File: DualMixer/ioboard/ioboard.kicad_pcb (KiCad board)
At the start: 2 copper layers, 35.6 x 107.9 mm, 22 parts, among them J1 IN_A1, J10 IN_B4, J11 OUTB, J13 Conn_01x03_Male, J2 IN_A2, J3 IN_A3, J4 OUTA, J5 Conn_02x07_Odd_Even, J6 IN_A4, J7 IN_B1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

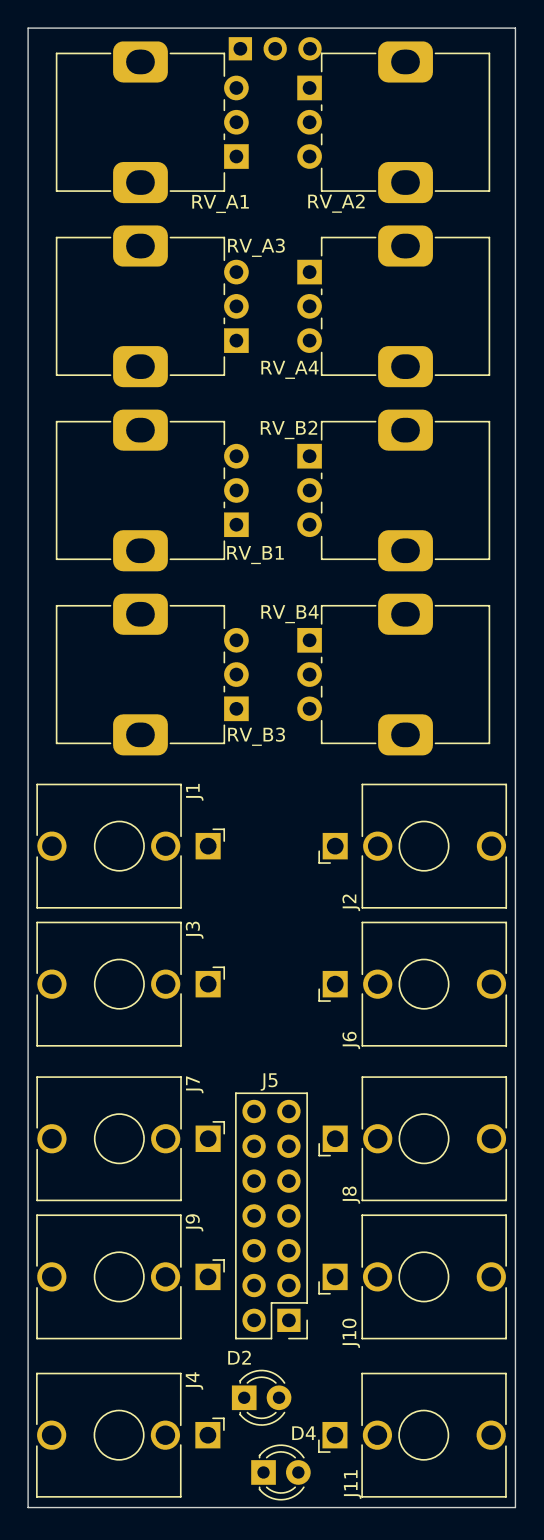
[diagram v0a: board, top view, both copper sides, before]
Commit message: Routed ioboard, add markings to mainboard
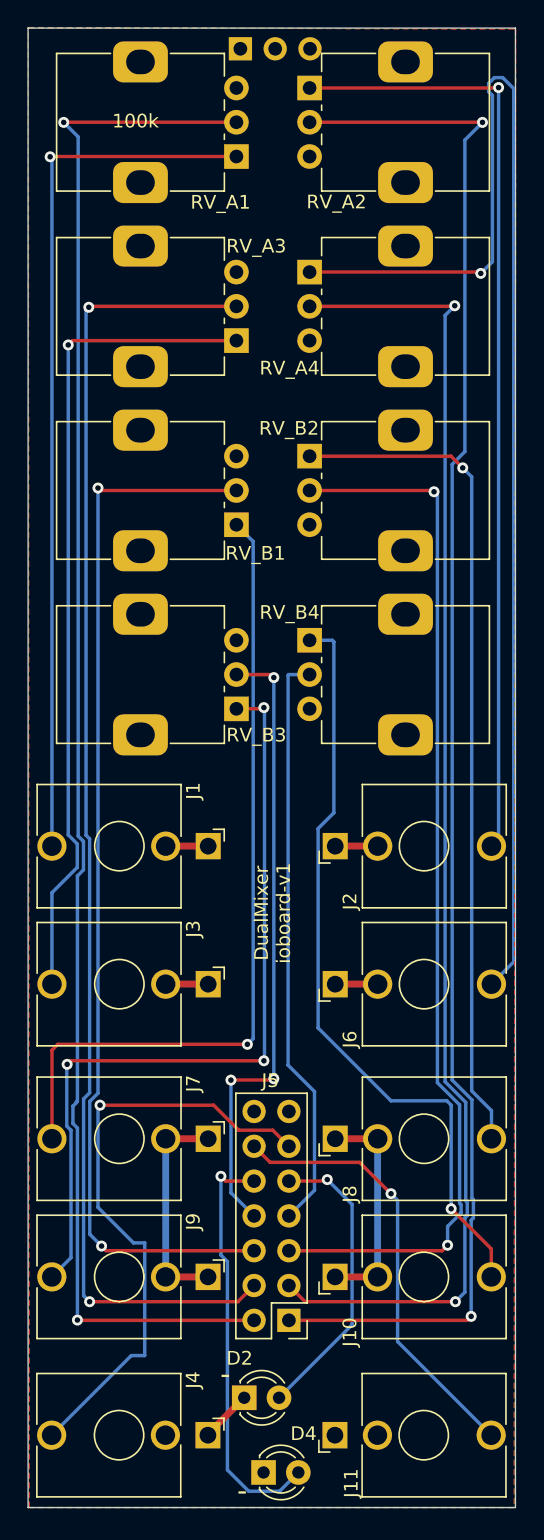
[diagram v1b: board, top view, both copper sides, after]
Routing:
- net /IN_A2: track 0.00 -> 114.8 mm, vias 0 -> 2
- net /IN_A1: track 0.00 -> 113.9 mm, vias 0 -> 2
- net /IN_A4: track 0.00 -> 97.2 mm, vias 0 -> 2
- net /IN_A3: track 0.00 -> 96.4 mm, vias 0 -> 2
- net Net-(J6-PadT): track 0.00 -> 95.2 mm, vias 0 -> 1
- net /IN_B1: track 0.00 -> 77.4 mm, vias 0 -> 2
- net /IN_B2: track 0.00 -> 77.1 mm, vias 0 -> 2
- net Net-(J2-PadT): track 0.00 -> 69.4 mm, vias 0 -> 1
- net Net-(J1-PadT): track 0.00 -> 64.0 mm, vias 0 -> 1
- net Net-(J8-PadT): track 0.00 -> 61.3 mm, vias 0 -> 1
- net Net-(J3-PadT): track 0.00 -> 60.1 mm, vias 0 -> 1
- net Net-(J7-PadT): track 0.00 -> 59.5 mm, vias 0 -> 1
- net Net-(J9-PadT): track 0.00 -> 58.5 mm, vias 0 -> 3
- net Net-(J10-PadT): track 0.00 -> 56.3 mm, vias 0 -> 1
- net GND: track 0.00 -> 48.8 mm
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- added copper zone on F.Cu, net GND
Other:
- board text added: "-"
- board text added: "DualMixer ioboard-v1"

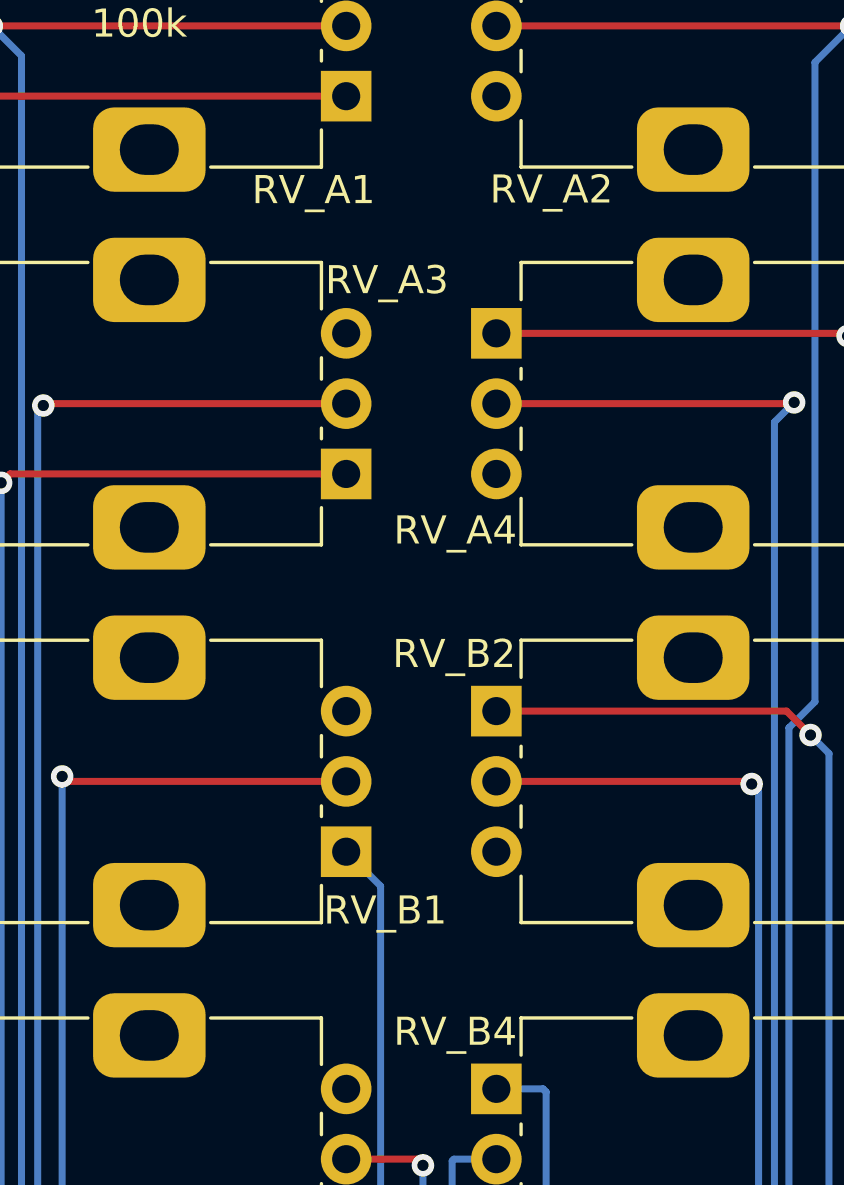
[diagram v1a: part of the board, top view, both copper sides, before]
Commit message: Add M3 mount for mechanical stability, and update power
This time for the DualMixer as well, it could do with extra supports
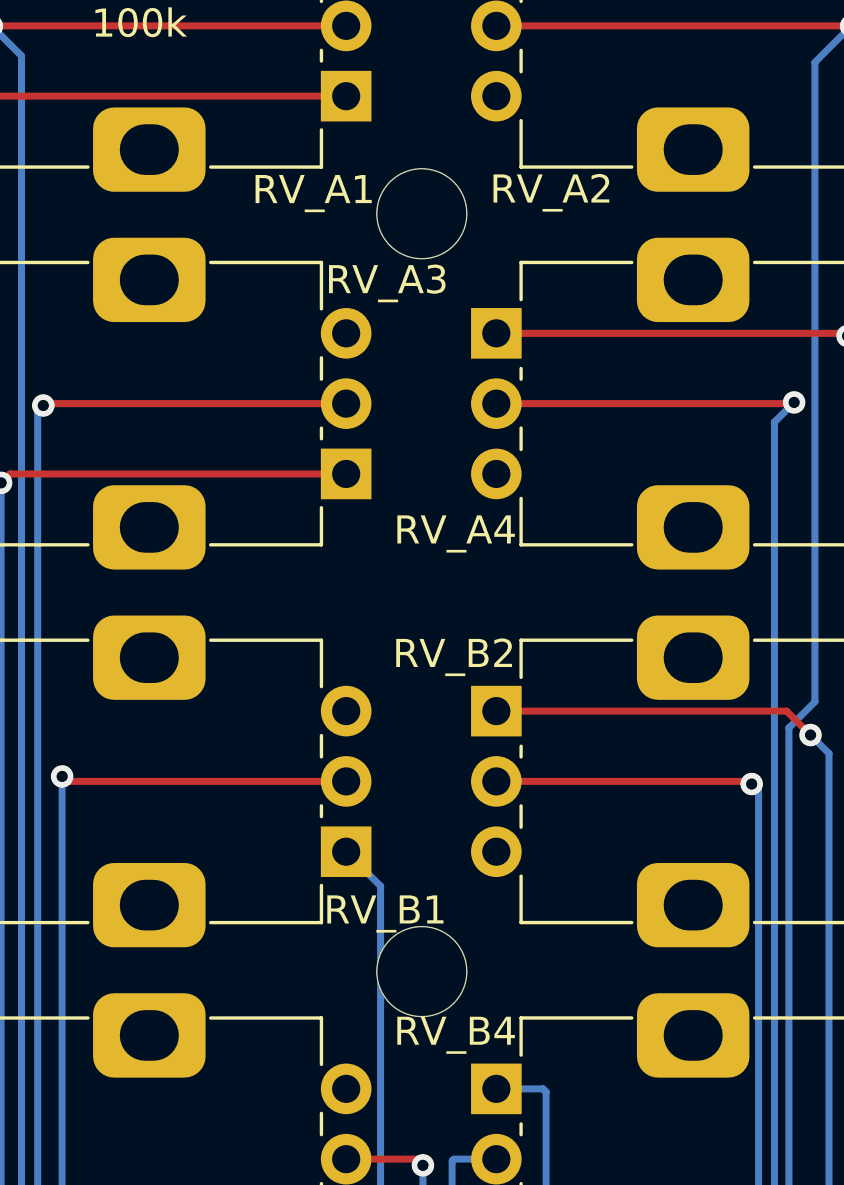
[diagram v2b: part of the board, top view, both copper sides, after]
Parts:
- added REF**: MountingHole_3.2mm_M3_NoCourt, Library:MountingHole_3.2mm_M3_NoCourt, F.Cu at (80.7, 79.7)
- added REF**: MountingHole_3.2mm_M3_NoCourt, Library:MountingHole_3.2mm_M3_NoCourt, F.Cu at (80.7, 52.7)
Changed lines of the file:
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@@
     )
+  )
+  (footprint "Library:MountingHole_3.2mm_M3_NoCourt" (layer "F.Cu")
+    (at 80.7 79.65)
+    (descr "Mounting Hole 3.2mm, no annular, M3")
+    (tags "mounting hole 3.2mm no annular m3")
+    (attr exclude_from_pos_files exclude_from_bom)
+    (fp_text reference "REF**" (at 0 -4.2) (layer "F.SilkS") hide
+      (effects (font (size 1 1) (thickness 0.15)))
+    )
+    (fp_text value "MountingHole_3.2mm_M3_NoCourt" (at 0 4.2) (layer "F.Fab")
+      (effects (font (size 1 1) (thickness 0.15)))
+    )
+    (fp_text user "${REFERENCE}" (at 0 0) (layer "F.Fab")
+      (effects (font (size 1 1) (thickness 0.15)))
+    )
+    (fp_circle (center 0 0) (end 1.61 0) (layer "F.CrtYd") (width 0.05) (fill none))
+    (pad "" np_thru_hole circle (at 0 0) (size 3.2 3.2) (drill 3.2) (layers *.Cu *.Mask))
   )
   (footprint "LED_THT:LED_D3.0mm" (layer "F.Cu")
@@
     )
   )
+  (footprint "Library:MountingHole_3.2mm_M3_NoCourt" (layer "F.Cu")
+    (at 80.7 52.7)
+    (descr "Mounting Hole 3.2mm, no annular, M3")
+    (tags "mounting hole 3.2mm no annular m3")
+    (attr exclude_from_pos_files exclude_from_bom)
+    (fp_text reference "REF**" (at 0 -4.2) (layer "F.SilkS") hide
+      (effects (font (size 1 1) (thickness 0.15)))
+    )
+    (fp_text value "MountingHole_3.2mm_M3_NoCourt" (at 0 4.2) (layer "F.Fab")
+      (effects (font (size 1 1) (thickness 0.15)))
+    )
+    (fp_text user "${REFERENCE}" (at 0 0) (layer "F.Fab")
+      (effects (font (size 1 1) (thickness 0.15)))
+    )
+    (fp_circle (center 0 0) (end 1.61 0) (layer "F.CrtYd") (width 0.05) (fill none))
+    (pad "" np_thru_hole circle (at 0 0) (size 3.2 3.2) (drill 3.2) (layers *.Cu *.Mask))
+  )
   (footprint "Connector_Audio:Jack_3.5mm_QingPu_WQP-PJ398SM_Vertical_CircularHoles" (layer "F.Cu")

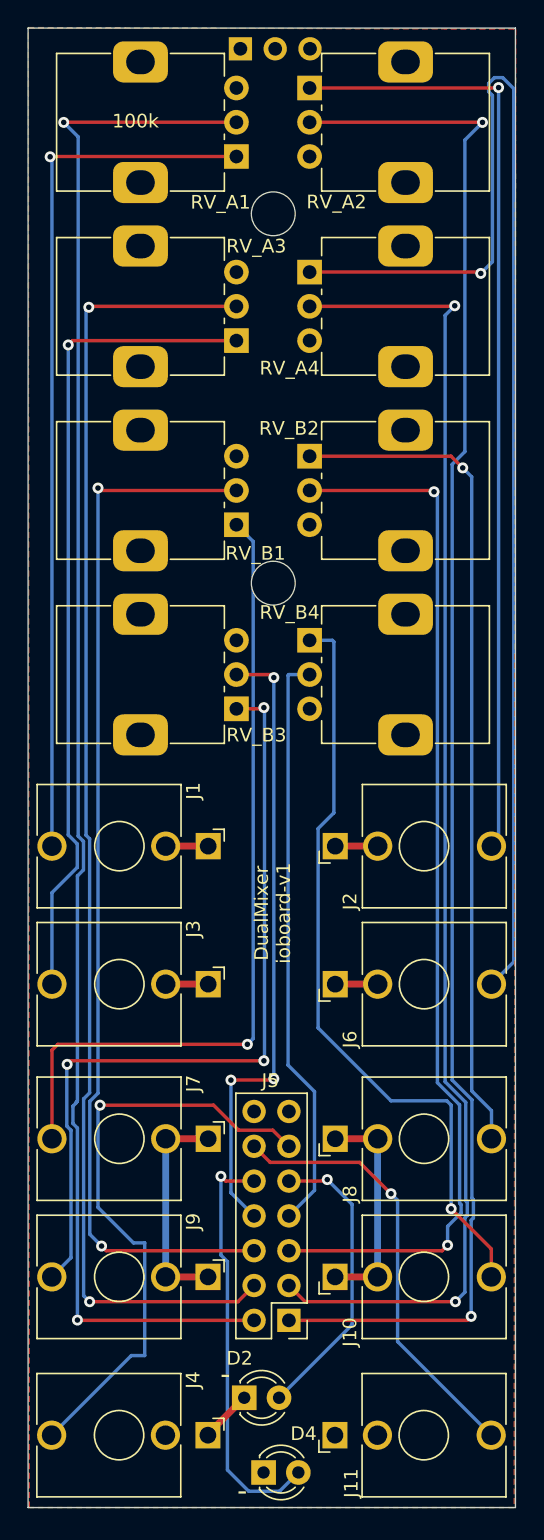
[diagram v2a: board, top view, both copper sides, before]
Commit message: Add extra ioboard + mainboard holes securing connection
So the two boards don't separate after installation.
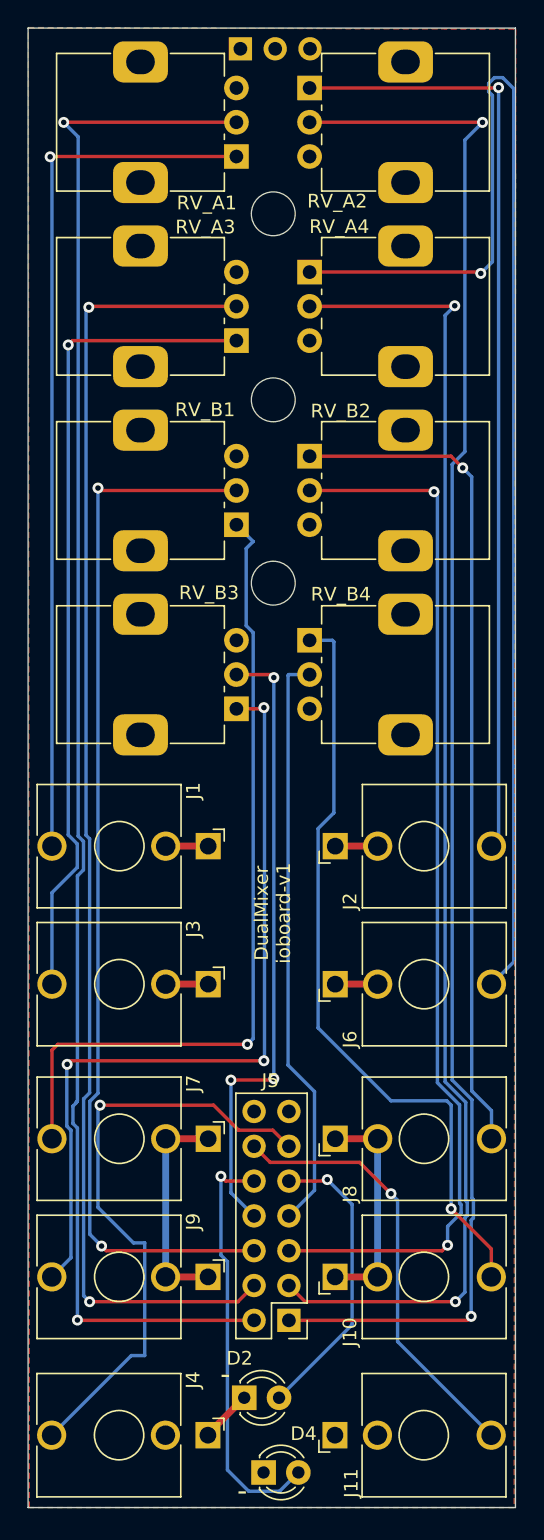
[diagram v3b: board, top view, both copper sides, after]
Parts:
- added REF**: MountingHole_3.2mm_M3_NoCourt, Library:MountingHole_3.2mm_M3_NoCourt, F.Cu at (80.7, 66.3)
- RV_A1, RV_A2, RV_A3, RV_A4, RV_B1, RV_B2, RV_B3, RV_B4: footprint Potentiometer_THT:Potentiometer_Alps_RK09K_Single_Vertical -> Library:Potentiometer_Alps_RK09K_Single_Vertical_MiniCourt

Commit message: Apply fixes for DualMixer rev1 module
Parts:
- RV_A1, RV_A2, RV_A3, RV_A4, RV_B1, RV_B2, RV_B3, RV_B4: footprint Library:Potentiometer_Alps_RK09K_Single_Vertical_MiniCourt -> Potentiometer_THT:Potentiometer_Alps_RK09K_Single_Vertical
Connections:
- RV_A1 pad 1: Net-(J1-PadT) -> GND
- RV_A1 pad 3: GND -> Net-(J1-PadT)
- RV_A2 pad 1: Net-(J2-PadT) -> GND
- RV_A2 pad 3: GND -> Net-(J2-PadT)
- RV_A3 pad 1: Net-(J3-PadT) -> GND
- RV_A3 pad 3: GND -> Net-(J3-PadT)
- RV_A4 pad 1: Net-(J6-PadT) -> GND
- RV_A4 pad 3: GND -> Net-(J6-PadT)
- RV_B1 pad 1: Net-(J7-PadT) -> GND
- RV_B1 pad 3: GND -> Net-(J7-PadT)
- RV_B2 pad 1: Net-(J8-PadT) -> GND
- RV_B2 pad 3: GND -> Net-(J8-PadT)
- RV_B3 pad 1: Net-(J9-PadT) -> GND
- RV_B3 pad 3: GND -> Net-(J9-PadT)
- RV_B4 pad 1: Net-(J10-PadT) -> GND
- RV_B4 pad 3: GND -> Net-(J10-PadT)
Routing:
- net Net-(J10-PadT): track 56.3 -> 50.3 mm
- net Net-(J7-PadT): track 59.9 -> 65.2 mm
- net Net-(J9-PadT): track 58.5 -> 62.2 mm, vias 3 -> 2
- net Net-(J2-PadT): track 69.4 -> 72.9 mm
- net /IN_A1: track 113.9 -> 111.7 mm
- net Net-(J3-PadT): track 60.1 -> 62.2 mm
- net Net-(J6-PadT): track 95.2 -> 97.3 mm
- net Net-(J1-PadT): track 64.0 -> 66.0 mm
- net Net-(J8-PadT): track 61.3 -> 63.1 mm
- net /IN_A3: track 96.4 -> 95.1 mm
